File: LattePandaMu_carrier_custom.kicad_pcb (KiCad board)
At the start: 4 copper layers, 170.1 x 100 mm, 217 parts, among them J1 Conn_01x03_Pin, J10 Conn_01x03_Pin, J11 Conn_01x03_Pin, J12 Conn_01x04_Pin, J13 Conn_01x04_Pin, J14 Conn_01x03_Pin, J15 Bus_M.2_Socket_M, J16 Bus_M.2_Socket_E, J17 Barrel_Jack_Switch, J18 USB_C_Receptacle_USB2.0_16P, J19 Conn_01x04_Pin, J20 Conn_01x04_Pin, J21 Conn_01x04_Pin, J3 HDMI_A, J4 USB3_A_Stacked, J5 USB_A_Stacked, J6 RJ45_RB1-125B8G1A, J7 Conn_01x04_Pin, J8 Conn_01x03_Pin, J9 Conn_01x04_Pin, M1 Fan_4pin, Q1 2N7002, Q2 2SK3018, Q3 2SK3018, Q4 2SK3018, Q8 2N7002, SW1 SW_Push, SW2 SW_Push, U1 D3V3XA4B10LP, U10 ULC0524P, U11 ULC0524P, U12 ULC0524P, U14 USB PD-CH224K-ESSOP10, U15 LM2734X, U16 LM2734X, U17 ULC0524P, U2 D3V3XA4B10LP, U3 D3V3XA4B10LP, U4 D3V3XA4B10LP, U5 D3V3XA4B10LP, U6 RTL8111H-CG-RH, U7 D3V3XA4B10LP, U8 D3V3XA4B10LP, U9 ULC0524P, Y1 25MHz

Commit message: finished placement
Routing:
- net /Power Supply/PWR_C_D+: track 13.4 -> 8.64 mm

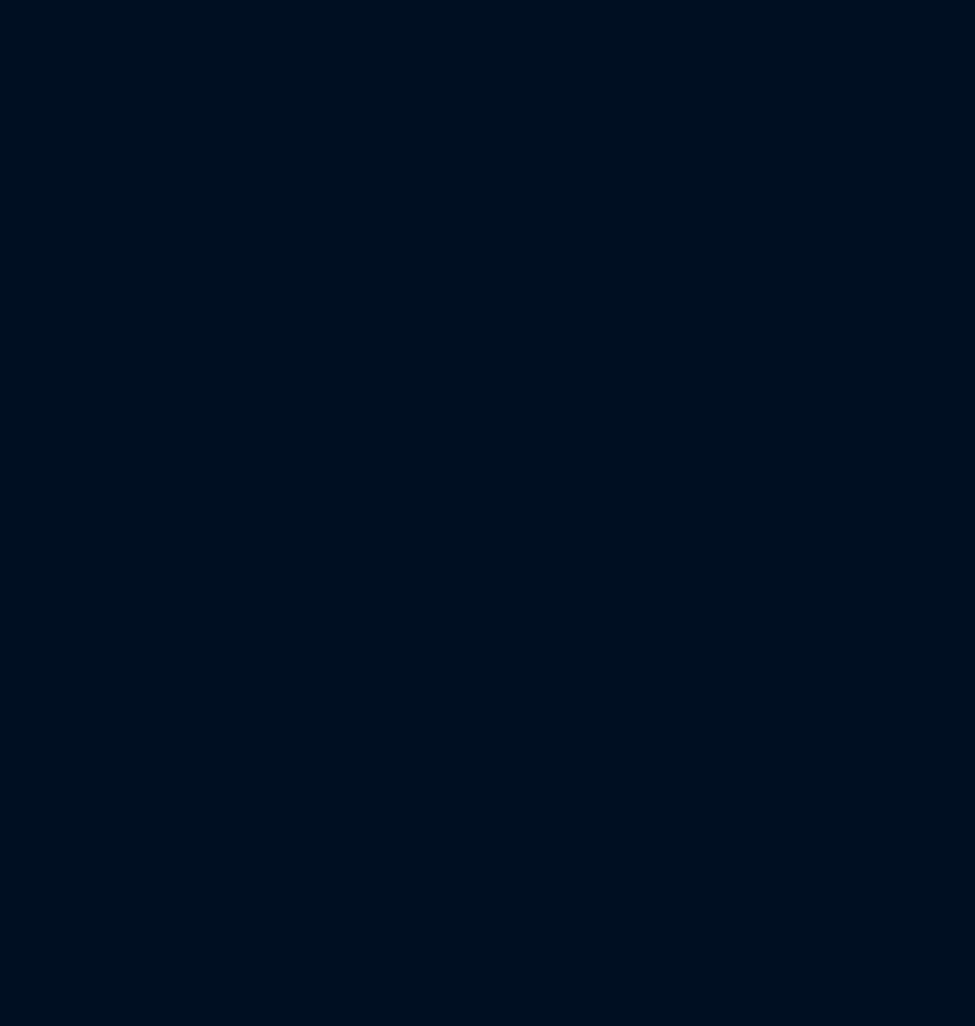
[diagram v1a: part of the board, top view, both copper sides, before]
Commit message: added pcie to schematic
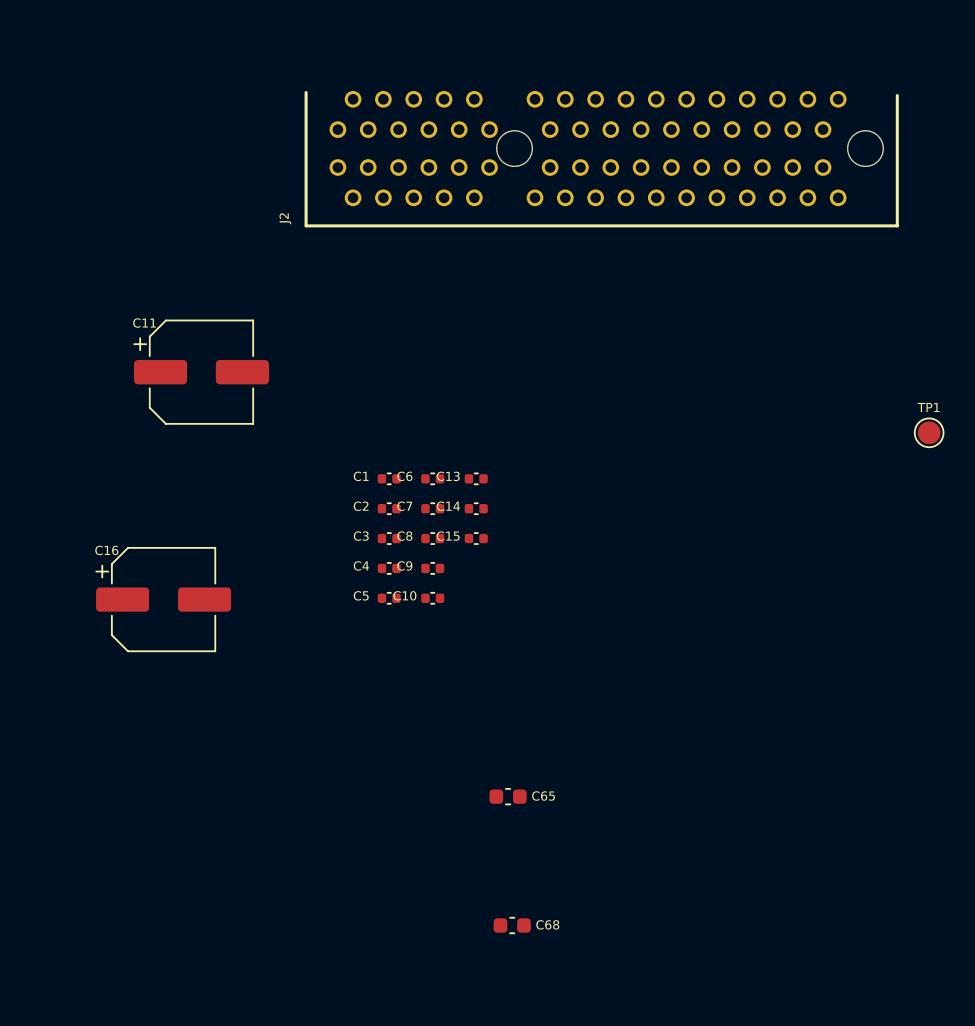
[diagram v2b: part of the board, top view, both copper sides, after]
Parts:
- added C1: 220nF/50V, A_HDJ_Library:C_0402_1005Metric, F.Cu at (339.4, 86.0)
- added C10: 100nF/50V, A_HDJ_Library:C_0402_1005Metric, F.Cu at (342.3, 93.9)
- added C11: 100uF/25V, A_HDJ_Library:CP_Elec_6.3x7.7, F.Cu at (327.0, 79.0)
- added C13: 100nF/50V, A_HDJ_Library:C_0402_1005Metric, F.Cu at (345.1, 86.0)
- added C14: 10uF/10V, A_HDJ_Library:C_0402_1005Metric, F.Cu at (345.1, 88.0)
- added C15: 100nF/50V, A_HDJ_Library:C_0402_1005Metric, F.Cu at (345.1, 90.0)
- added C16: 560uF/25V, A_HDJ_Library:CP_Elec_6.3x7.7, F.Cu at (324.5, 94.0)
- added C2: 220nF/50V, A_HDJ_Library:C_0402_1005Metric, F.Cu at (339.4, 88.0)
- added C3: 220nF/50V, A_HDJ_Library:C_0402_1005Metric, F.Cu at (339.4, 90.0)
- added C4: 220nF/50V, A_HDJ_Library:C_0402_1005Metric, F.Cu at (339.4, 91.9)
- added C5: 220nF/50V, A_HDJ_Library:C_0402_1005Metric, F.Cu at (339.4, 93.9)
- added C6: 220nF/50V, A_HDJ_Library:C_0402_1005Metric, F.Cu at (342.3, 86.0)
- added C65: 22uF/10V, A_HDJ_Library:C_0603_1608Metric, F.Cu at (347.2, 107.0)
- added C68: 22uF/10V, A_HDJ_Library:C_0603_1608Metric, F.Cu at (347.5, 115.5)
- added C7: 220nF/50V, A_HDJ_Library:C_0402_1005Metric, F.Cu at (342.3, 88.0)
- added C8: 220nF/50V, A_HDJ_Library:C_0402_1005Metric, F.Cu at (342.3, 90.0)
- added C9: 100nF/50V, A_HDJ_Library:C_0402_1005Metric, F.Cu at (342.3, 91.9)
- added J2: Bus_PCI_Express_x4, A_HDJ_Library:PCIe_x4_Gen3Slot_Connectors, F.Cu at (336.0, 63.0)
- added TP1: TestPoint, A_HDJ_Library:TestPoint_Pad_D1.5mm, F.Cu at (375.0, 83.0)
- U14: value USB PD-CH224K-ESSOP10 -> USB PD等快充协议受电芯片-CH224K-ESSOP10
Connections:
- A1 pad 7: /LattePanda Module/SLS_S3 -> VDC
- JP1 pad 2: Net-(JP1-C) -> VDC
- JP1 pad 3: /LattePanda Module/SLS_S3 -> VDC
- R46 pad 2: Net-(JP1-C) -> VDC
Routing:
- net VDC: track 133.7 -> 263.0 mm, vias 86 -> 88
- net /LattePanda Module/SLS_S3: track 115.6 -> 0.00 mm, vias 2 -> 0
- net Net-(JP1-C): track 13.7 -> 0.00 mm
